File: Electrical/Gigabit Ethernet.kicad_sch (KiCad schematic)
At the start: 54 parts, among them IC1 RTL8125BG-CG, IC4 RTL8125BG-CG, J11 SS-60300-011, J2 SS-60300-011, Y1 25MHz, Y4 25MHz

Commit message: Major Overhaul
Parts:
- C126, C132, C134, C137, C138, C33, C34, C36, C37, C39, C40, C44, C45, C46, C47, C55, C56, C61, C69, C85, C86, C87, C88, C89: value C -> 100nF/50v
- C129, C130, C131, C133, C135, C136, C35, C38, C41, C42: value 10uF/10V -> 100nF/50v
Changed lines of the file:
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@@
 	)
 	(hierarchical_label "GbE_PCIe_1_RX-"
-		(shape input)
+		(shape output)
 		(at 374.65 260.35 180)
 		(effects
@@
 	)
 	(hierarchical_label "GbE_PCIe_0_TX-"
-		(shape output)
+		(shape input)
 		(at 142.24 269.24 180)
 		(effects
@@
 	)
 	(hierarchical_label "GbE_PCIe_1_RX+"
-		(shape input)
+		(shape output)
 		(at 374.65 255.27 180)
 		(effects
@@
 	)
 	(hierarchical_label "GbE_PCIe_0_RX-"
-		(shape input)
+		(shape output)
 		(at 142.24 261.62 180)
 		(effects
@@
 	)
 	(hierarchical_label "GbE_PCIe_1_TX-"
-		(shape output)
+		(shape input)
 		(at 378.46 267.97 180)
 		(effects
@@
 	)
 	(hierarchical_label "GbE_PCIe_0_RX+"
-		(shape input)
+		(shape output)
 		(at 134.62 256.54 180)
 		(effects
@@
 	)
 	(hierarchical_label "GbE_PCIe_0_TX+"
-		(shape output)
+		(shape input)
 		(at 142.24 266.7 180)
 		(effects
@@
 	)
 	(hierarchical_label "GbE_PCIe_1_TX+"
-		(shape output)
+		(shape input)
 		(at 378.46 265.43 180)
 		(effects
@@
 			)
 		)
-		(property "Value" "C"
+		(property "Value" "100nF/50v"
 			(at 392.43 250.19 90)
 			(effects
@@
 			)
 		)
-		(property "Value" "C"
+		(property "Value" "100nF/50v"
 			(at 455.93 232.4099 0)
 			(effects
@@
 			)
 		)
-		(property "Value" "C"
+		(property "Value" "100nF/50v"
 			(at 116.84 284.48 90)
 			(effects
@@
 			)
 		)
-		(property "Value" "C"
+		(property "Value" "100nF/50v"
 			(at 123.19 284.48 90)
 			(effects
@@
 			)
 		)
-		(property "Value" "C"
+		(property "Value" "100nF/50v"
 			(at 482.6 294.64 90)
 			(effects
@@
 			)
 		)
-		(property "Value" "C"
+		(property "Value" "100nF/50v"
 			(at 388.62 260.35 90)
 			(effects
@@
 			)
 		)
-		(property "Value" "10uF/10V"
+		(property "Value" "100nF/50v"
 			(at 393.7 290.83 90)
 			(effects
@@
 			)
 		)
-		(property "Value" "C"
+		(property "Value" "100nF/50v"
 			(at 156.21 251.46 90)
 			(effects
@@
 			)
 		)
-		(property "Value" "C"
+		(property "Value" "100nF/50v"
 			(at 205.74 217.17 90)
 			(effects
@@
 			)
 		)
-		(property "Value" "10uF/10V"
+		(property "Value" "100nF/50v"
 			(at 152.4 292.1 90)
 			(effects
@@
 			)
 		)
-		(property "Value" "C"
+		(property "Value" "100nF/50v"
 			(at 205.74 228.6 90)
 			(effects
@@
 			)
 		)
-		(property "Value" "C"
+		(property "Value" "100nF/50v"
 			(at 441.96 215.9 90)
 			(effects
@@
 			)
 		)
-		(property "Value" "C"
+		(property "Value" "100nF/50v"
 			(at 394.97 262.89 90)
 			(effects
@@
 			)
 		)
-		(property "Value" "C"
+		(property "Value" "100nF/50v"
 			(at 359.41 283.21 90)
 			(effects
@@
 			)
 		)
-		(property "Value" "10uF/10V"
+		(property "Value" "100nF/50v"
 			(at 157.48 292.1 90)
 			(effects
@@
 			)
 		)
-		(property "Value" "C"
+		(property "Value" "100nF/50v"
 			(at 353.06 283.21 90)
 			(effects
@@
 			)
 		)
-		(property "Value" "C"
+		(property "Value" "100nF/50v"
 			(at 160.02 256.54 90)
 			(effects
@@
 			)
 		)
-		(property "Value" "C"
+		(property "Value" "100nF/50v"
 			(at 158.75 264.16 90)
 			(effects
@@
 			)
 		)
-		(property "Value" "10uF/10V"
+		(property "Value" "100nF/50v"
 			(at 477.52 257.81 90)
 			(effects
@@
 			)
 		)
-		(property "Value" "10uF/10V"
+		(property "Value" "100nF/50v"
 			(at 241.3 259.08 90)
 			(effects
@@
 			)
 		)
-		(property "Value" "C"
+		(property "Value" "100nF/50v"
 			(at 205.74 223.52 90)
 			(effects
@@
 			)
 		)
-		(property "Value" "10uF/10V"
+		(property "Value" "100nF/50v"
 			(at 388.62 290.83 90)
 			(effects
@@
 			)
 		)
-		(property "Value" "10uF/10V"
+		(property "Value" "100nF/50v"
 			(at 246.38 259.08 90)
 			(effects
@@
 			)
 		)
-		(property "Value" "C"
+		(property "Value" "100nF/50v"
 			(at 246.38 295.91 90)
 			(effects
@@
 			)
 		)
-		(property "Value" "10uF/10V"
+		(property "Value" "100nF/50v"
 			(at 440.69 314.96 90)
 			(effects
@@
 			)
 		)
-		(property "Value" "C"
+		(property "Value" "100nF/50v"
 			(at 482.6 288.29 90)
 			(effects
@@
 			)
 		)
-		(property "Value" "C"
+		(property "Value" "100nF/50v"
 			(at 246.38 289.56 90)
 			(effects
@@
 			)
 		)
-		(property "Value" "C"
+		(property "Value" "100nF/50v"
 			(at 396.24 255.27 90)
 			(effects
@@
 			)
 		)
-		(property "Value" "10uF/10V"
+		(property "Value" "100nF/50v"
 			(at 485.648 250.952 90)
 			(effects
@@
 			)
 		)
-		(property "Value" "C"
+		(property "Value" "100nF/50v"
 			(at 152.4 261.62 90)
 			(effects
@@
 			)
 		)
-		(property "Value" "C"
+		(property "Value" "100nF/50v"
 			(at 219.71 233.6799 0)
 			(effects
@@
 			)
 		)
-		(property "Value" "C"
+		(property "Value" "100nF/50v"
 			(at 441.96 227.33 90)
 			(effects
@@
 			)
 		)
-		(property "Value" "C"
+		(property "Value" "100nF/50v"
 			(at 441.96 222.25 90)
 			(effects
@@
 			)
 		)
-		(property "Value" "10uF/10V"
+		(property "Value" "100nF/50v"
 			(at 435.61 314.96 90)
 			(effects

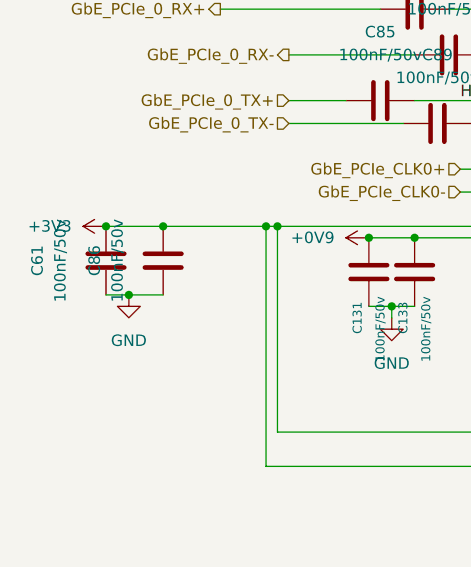
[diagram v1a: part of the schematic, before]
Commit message: Fix Ground Plane Intteruptions
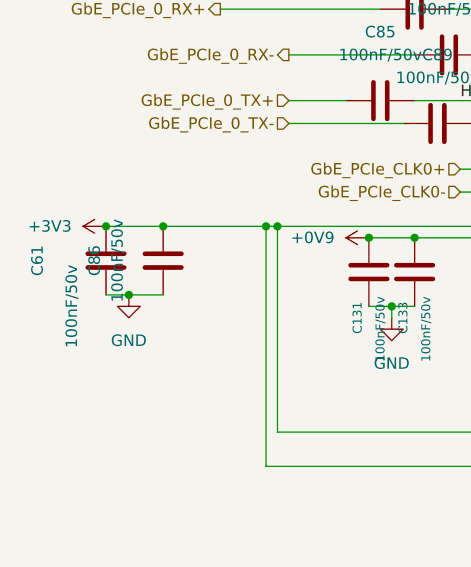
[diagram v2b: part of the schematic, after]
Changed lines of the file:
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@@
 		(on_board yes)
 		(dnp no)
-		(fields_autoplaced yes)
 		(property "Reference" "C61"
 			(at 114.3 284.48 90)
@@
 		)
 		(property "Value" "100nF/50v"
-			(at 116.84 284.48 90)
+			(at 118.11 289.56 90)
 			(effects
 				(font

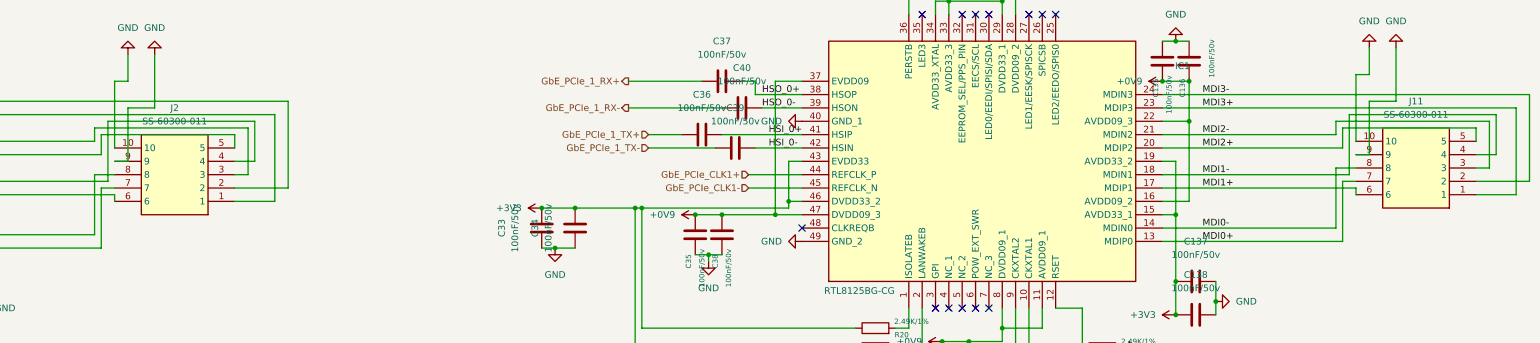
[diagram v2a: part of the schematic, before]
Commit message: Update Board According to DFA Review
Updated Ethernet Jack
Updated L3 Inductor
Fixed a few errors
Updated mounting hole size
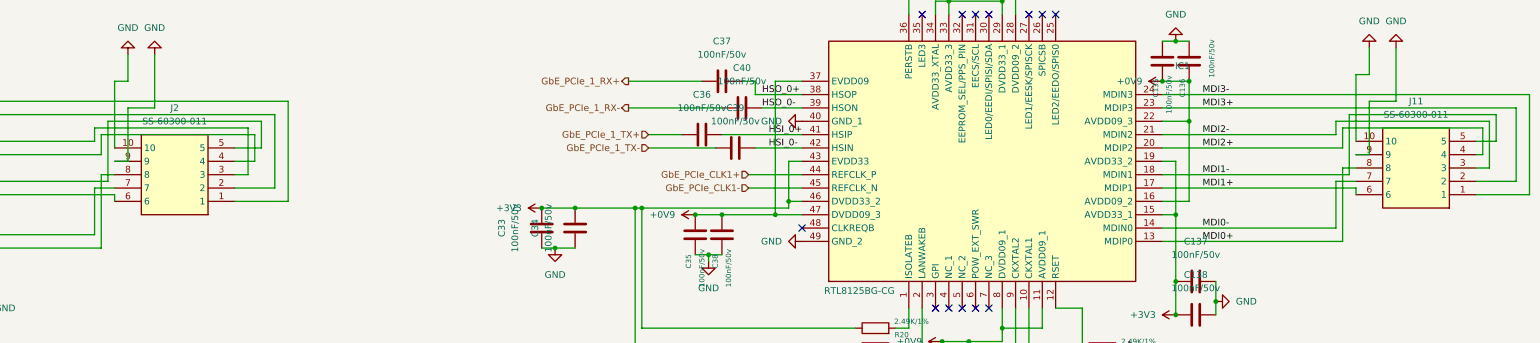
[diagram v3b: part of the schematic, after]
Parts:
- J11, J2: footprint SS60300011 -> ethernet:438600010
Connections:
- net MDI0+: now also J11.8; no longer J11.7
- net MDI0-: now also J11.7; no longer J11.8
- net MDI1-: now also J11.5; no longer J11.4
- net MDI2+: now also J11.4; no longer J11.5
- net MDI3+: now also J11.2; no longer J11.1
- net MDI3-: now also J11.1; no longer J11.2
- net MDI_0+: now also J2.8; no longer J2.7
- net MDI_0-: now also J2.7; no longer J2.8
- net MDI_1-: now also J2.5; no longer J2.4
- net MDI_2+: now also J2.4; no longer J2.5
- net MDI_3+: now also J2.2; no longer J2.1
- net MDI_3-: now also J2.1; no longer J2.2

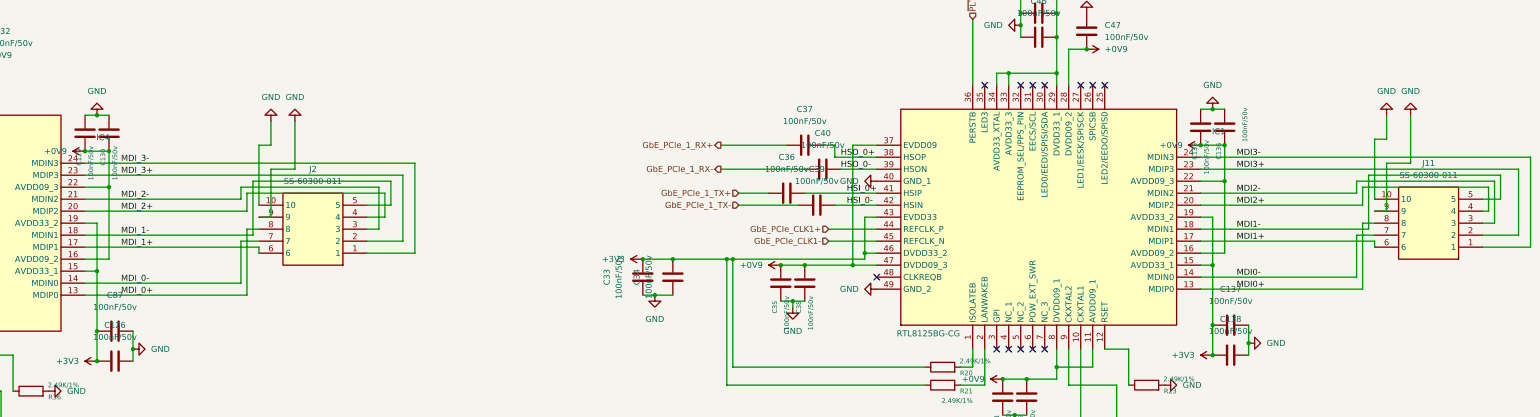
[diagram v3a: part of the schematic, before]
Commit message: Further DFA Changes
Changed RJ45 jack to one capable of 10gbps, to remove any possible bottleneck
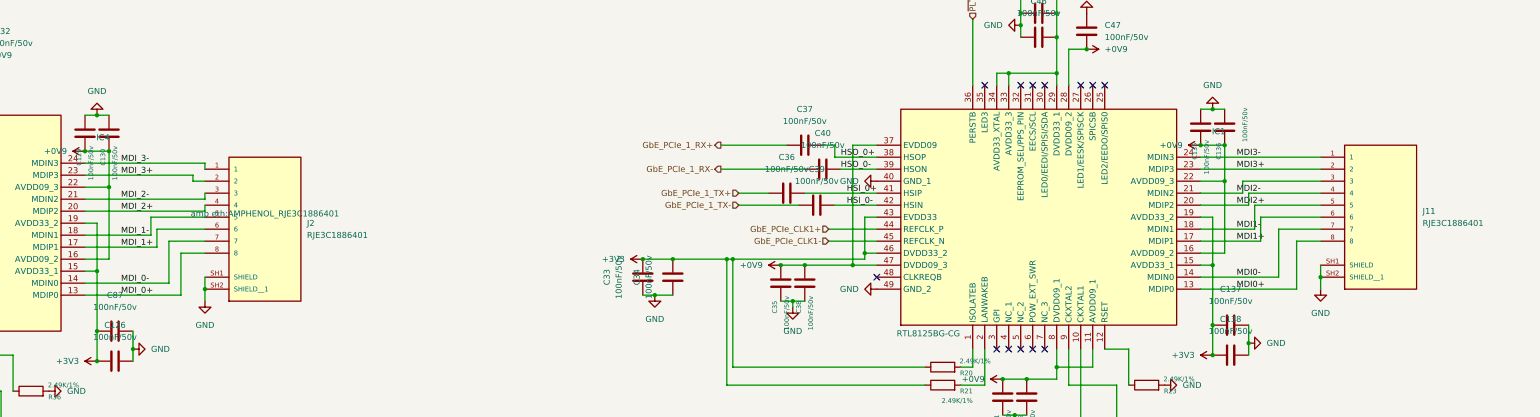
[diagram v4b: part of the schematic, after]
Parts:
- removed J11, J2: SS-60300-011, ethernet:438600010, symbol 2.5g ethernet:SS-60300-011
- added J11, J2: RJE3C1886401, amp eth:AMPHENOL_RJE3C1886401, symbol amp eth:RJE3C1886401
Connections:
- net GND: now also J11.SH1 (SHIELD), J11.SH2 (SHIELD__1), J2.SH1 (SHIELD), J2.SH2 (SHIELD__1)
- net MDI0+: now also J11.8
- net MDI0-: now also J11.7
- net MDI1+: now also J11.6
- net MDI1-: now also J11.5
- net MDI2+: now also J11.4
- net MDI2-: now also J11.3
- net MDI3+: now also J11.2
- net MDI3-: now also J11.1
- net MDI_0+: now also J2.8
- net MDI_0-: now also J2.7
- net MDI_1+: now also J2.6
- net MDI_1-: now also J2.5
- net MDI_2+: now also J2.4
- net MDI_2-: now also J2.3
- net MDI_3+: now also J2.2
- net MDI_3-: now also J2.1
